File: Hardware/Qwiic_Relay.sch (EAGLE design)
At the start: 35 parts, among them J4 AVR_SPI_PROG_3X2TESTPOINTS, K1 RELAY-SPDT, Q4 600mA/40V, U1 ATTINY85_SOIC_5.3MM, U2 LTV-816_OPTO_ISOLATOR"

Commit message: pre review
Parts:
- R1: device SparkFun-Resistors:47KOHM-0603-1/10W-1% -> SparkFun-Resistors:10OHM-0603-1/10W-1%
- R2: device SparkFun-Resistors:100OHM-0603-1/4W-5% -> SparkFun-Resistors:100OHM-0603-1/10W-1%
- R4: device SparkFun-Resistors:300OHM-0603-1/10W-1% -> SparkFun-Resistors:330OHM-0603-1/10W-1%
- R6, R7: value 2.2K -> 2.2k; device SparkFun-Resistors:4.7KOHM-0603-1/10W-1% -> SparkFun-Resistors:2.2KOHM-0603-1/10W-1%
- R8: value 10K -> 10k; device SparkFun-Resistors:330OHM-0603-1/10W-1% -> SparkFun-Resistors:10KOHM-0603-1/10W-1%
- R9: device SparkFun-Resistors:330OHM-0603-1/10W-1% -> SparkFun-Resistors:1KOHM-0603-1/10W-1%
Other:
- note added: "JP7 is the I2C pullup jumper bus. Disconnect this jumper to disconnect the I2C pullup resistors. If you have many Qwiic boards chained on the same I2C bus to prevent unnecessary current draw."
- note added: "v10"
- note removed: "Screw Terminal"
- note removed: "v01"
- moved on the sheet: J1, J2, J3, J5

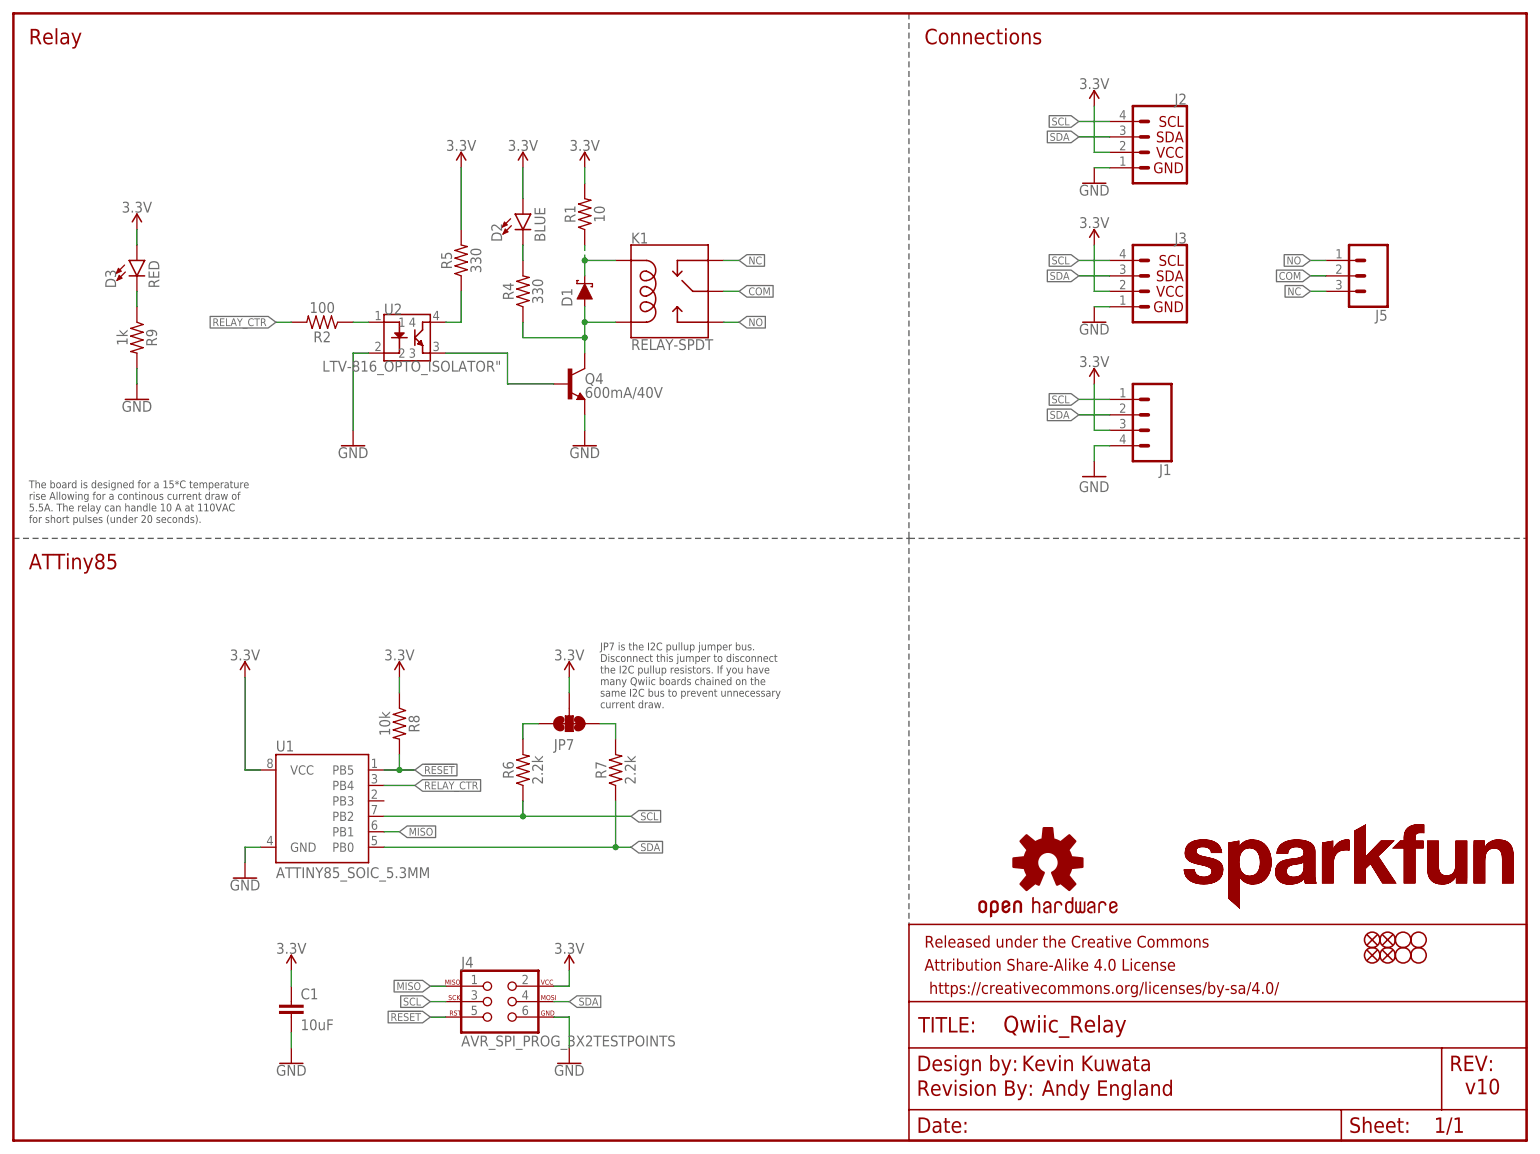
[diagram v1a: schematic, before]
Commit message: changing to most recent rev
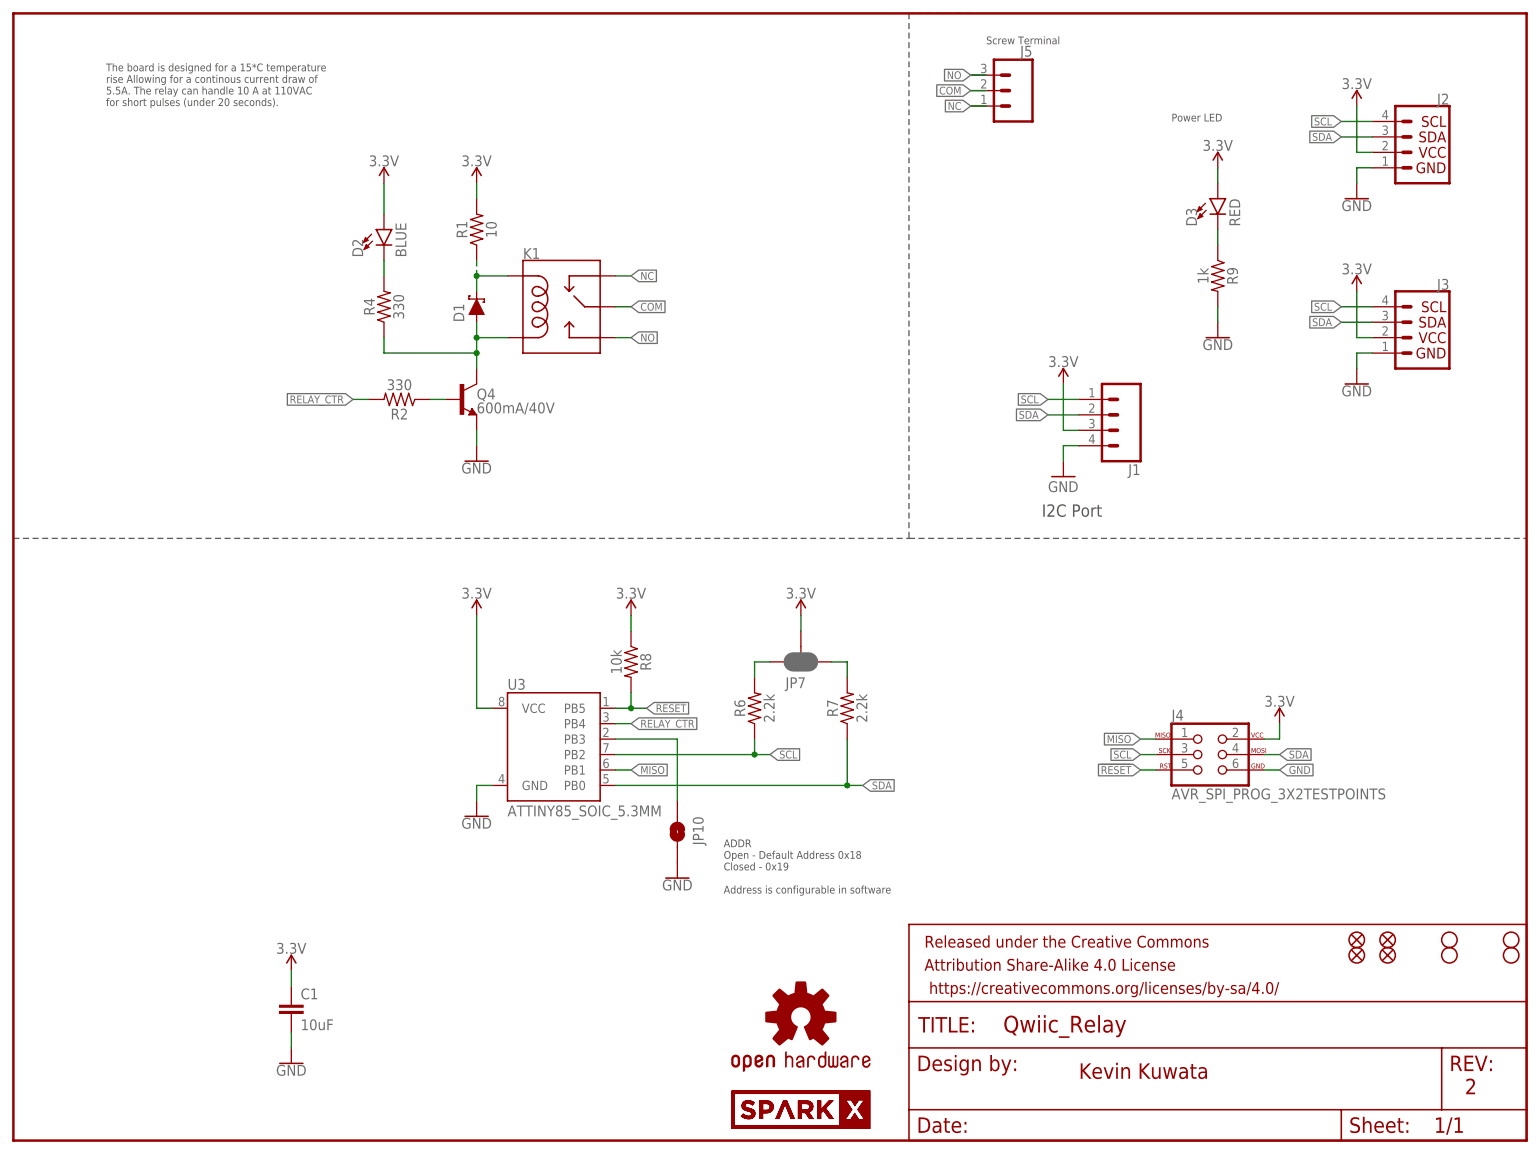
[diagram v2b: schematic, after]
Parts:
- removed LOGO2: REVISION, SparkFun-Aesthetics:REVISION
- removed R5: 330, SparkFun-Resistors:330OHM-0603-1/10W-1%
- removed U1: ATTINY85_SOIC_5.3MM, SparkFun-IC-Microcontroller:ATTINY85_SOIC_5.3MM
- removed U2: LTV-816_OPTO_ISOLATOR", SparkFun-DiscreteSemi:LTV-816_OPTO_ISOLATOR"
- added JP10: JUMPER-SMT_2_NO_NO-SILK, SparkFun-Jumpers:JUMPER-SMT_2_NO_NO-SILK
- added U3: ATTINY85_SOIC_5.3MM, SparkFun-IC-Microcontroller:ATTINY85_SOIC_5.3MM
- JP7: value JUMPER-SMT_3_2-NC_TRACE_NO-SILK -> JUMPER-SMT_3_2-NC_PASTE_SILK; device SparkFun-Jumpers:JUMPER-SMT_3_2-NC_TRACE_NO-SILK -> SparkFun-Jumpers:JUMPER-SMT_3_2-NC_PASTE_SILK
- K1: value RELAY-SPDT -> (none); device SparkFun-Electromechanical:RELAY-SPDT -> SparkX:RELAY_SPDT_1C
- R1: device SparkFun-Resistors:10OHM-0603-1/10W-1% -> SparkFun-Resistors:10OHM-0603-1/10W-5%
- R2: value 100 -> 330; device SparkFun-Resistors:100OHM-0603-1/10W-1% -> SparkFun-Resistors:330OHM-0603-1/10W-1%
- U$3, U$4: value SFE_LOGO_NAME.1_INCH -> SPARKX-LOGO4; device SparkFun-Aesthetics:SFE_LOGO_NAME.1_INCH -> SparkX:SPARKX-LOGO4
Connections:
- removed net N$3: R2.1, U2.1
- removed net N$9: R5.1, U2.4
- new net N$5: JP10.1, U3.PB3
- net !RESET: now also U3.PB5; no longer U1.PB5
- net 3.3V: now also U3.VCC; no longer R5.2, U1.VCC
- net GND: now also JP10.2, U3.GND; no longer U1.GND, U2.2
- net MISO: now also U3.PB1; no longer U1.PB1
- net N$1: now also R2.1; no longer U2.3
- net NC: now also J5.1; no longer J5.3
- net NO: now also J5.3; no longer J5.1
- net RELAY_CTR: now also U3.PB4; no longer U1.PB4
- net SCL: now also U3.PB2; no longer U1.PB2
- net SDA: now also U3.PB0; no longer U1.PB0
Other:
- note added: "2"
- note added: "ADDR Open - Default Address 0x18 Closed - 0x19 Address is configurable in software"
- note added: "I2C Port"
- note added: "Power LED"
- note added: "Screw Terminal"
- note removed: "ATTiny85"
- note removed: "Andy England"
- note removed: "Connections"
- note removed: "JP7 is the I2C pullup jumper bus. Disconnect this jumper to disconnect the I2C pullup resistors. If you have many Qwiic boards chained on the same I2C bus to prevent unnecessary current draw."
- note removed: "Relay"
- note removed: "v10"
- moved on the sheet: D1, D2, D3, J1, J2, J3, J4, J5, Q4, R1, R2, R4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

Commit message: pre review
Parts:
- added LOGO2: REVISION, SparkFun-Aesthetics:REVISION
- JP7: value JUMPER-SMT_3_2-NC_PASTE_SILK -> JUMPER-SMT_3_2-NC_TRACE_NO-SILK; device SparkFun-Jumpers:JUMPER-SMT_3_2-NC_PASTE_SILK -> SparkFun-Jumpers:JUMPER-SMT_3_2-NC_TRACE_NO-SILK
- K1: value (none) -> RELAY-SPDT; device SparkX:RELAY_SPDT_1C -> SparkFun-Electromechanical:RELAY-SPDT
- U$3: value SPARKX-LOGO4 -> SFE_LOGO_NAME.1_INCH; device SparkX:SPARKX-LOGO4 -> SparkFun-Aesthetics:SFE_LOGO_NAME.1_INCH
- U$4: value SPARKX-LOGO4 -> SFE_LOGO_NAME_FLAME.1_INCH; device SparkX:SPARKX-LOGO4 -> SparkFun-Aesthetics:SFE_LOGO_NAME_FLAME.1_INCH
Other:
- note added: "ATTiny85"
- note added: "Andy England"
- note added: "Connections"
- note added: "Disconnect jumper JP7 to disconnect the I2C pullup resistors."
- note added: "High Voltage on NC, COM and NO when AC is connected Coil Resistance: 23.5 Ohms"
- note added: "Relay"
- note added: "VCC: 1.8V-5.5V"
- note added: "v10"
- note removed: "2"
- note removed: "Power LED"
- moved on the sheet: C1, D3, J1, J2, J3, J4, J5, JP10, R6, R7, R8, R9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

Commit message: post review
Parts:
- U3: value ATTINY85_SOIC_5.3MM -> ATTINY85; device SparkFun-IC-Microcontroller:ATTINY85_SOIC_5.3MM -> SparkFun-IC-Microcontroller:ATTINY85
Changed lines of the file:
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@@
 <part name="GND9" library="SparkFun-PowerSymbols" deviceset="GND" device=""/>
 <part name="J5" library="SparkFun-Connectors" deviceset="CONN_03" device="-SCREW-5MM"/>
-<part name="U3" library="SparkFun-IC-Microcontroller" deviceset="ATTINY85" device="_SOIC_5.3MM"/>
+<part name="U3" library="SparkFun-IC-Microcontroller" deviceset="ATTINY85" device=""/>
 <part name="LOGO2" library="SparkFun-Aesthetics" deviceset="REVISION" device=""/>
 <part name="GND2" library="SparkFun-PowerSymbols" deviceset="GND" device=""/>
@@
 <instance part="JP7" gate="G$1" x="93.98" y="73.66" smashed="yes" rot="R270">
 <attribute name="NAME" x="91.44" y="69.342" size="1.778" layer="95" font="vector"/>
-<attribute name="VALUE" x="93.599" y="71.12" size="1.778" layer="96" font="vector" rot="R270" align="top-left"/>
 </instance>
 <instance part="SUPPLY9" gate="G$1" x="93.98" y="81.28"/>
-<instance part="J4" gate="G$1" x="68.58" y="20.32"/>
+<instance part="J4" gate="G$1" x="68.58" y="20.32" smashed="yes">
+<attribute name="NAME" x="63.5" y="25.908" size="1.778" layer="95" font="vector"/>
+</instance>
 <instance part="R8" gate="G$1" x="66.04" y="73.66" rot="R270"/>
 <instance part="SUPPLY10" gate="G$1" x="66.04" y="81.28"/>
